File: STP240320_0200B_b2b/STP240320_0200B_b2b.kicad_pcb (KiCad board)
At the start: 2 copper layers, 6.1 x 11.2 mm, 2 parts, among them J1 Conn_02x08_Odd_Even

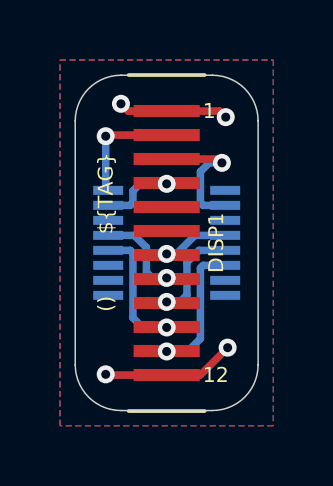
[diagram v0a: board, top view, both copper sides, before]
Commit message: all: cleanup revision info
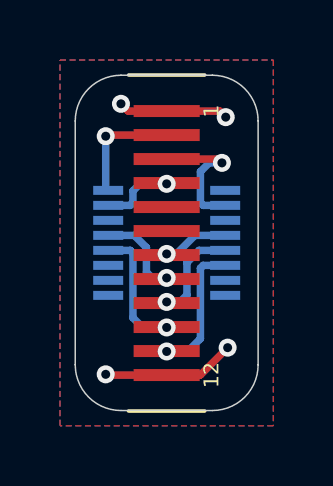
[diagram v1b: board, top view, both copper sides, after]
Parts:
- added SYM1: Logo_Open_Hardware_Large, Gigahawk:OSHW-Logo2_1.3x1.3mm_Mask, B.Cu at (116.4, 84.2)
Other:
- board text added: "JLCJLCJLCJLC"
- board text added: "STP240320_0200B B2B Adapter"
- board text added: "TAG (${HASH})"
- board text removed: "${TAG}"
- board text removed: "(${REVISION})"

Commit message: b2b: fix broken tag text
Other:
- board text added: "${TAG} (${HASH})"
- board text removed: "TAG (${HASH})"
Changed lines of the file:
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@@
     (effects (font (size 0.8 0.8) (thickness 0.15)) (justify mirror))
   )
-  (gr_text "TAG (${HASH})" (at 114.3 92.5 90) (layer "F.Mask")
+  (gr_text "${TAG} (${HASH})" (at 114.3 92.5 90) (layer "F.Mask")
     (effects (font (size 0.5 0.5) (thickness 0.1)) (justify left))
   )
